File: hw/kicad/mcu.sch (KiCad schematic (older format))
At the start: 38 parts

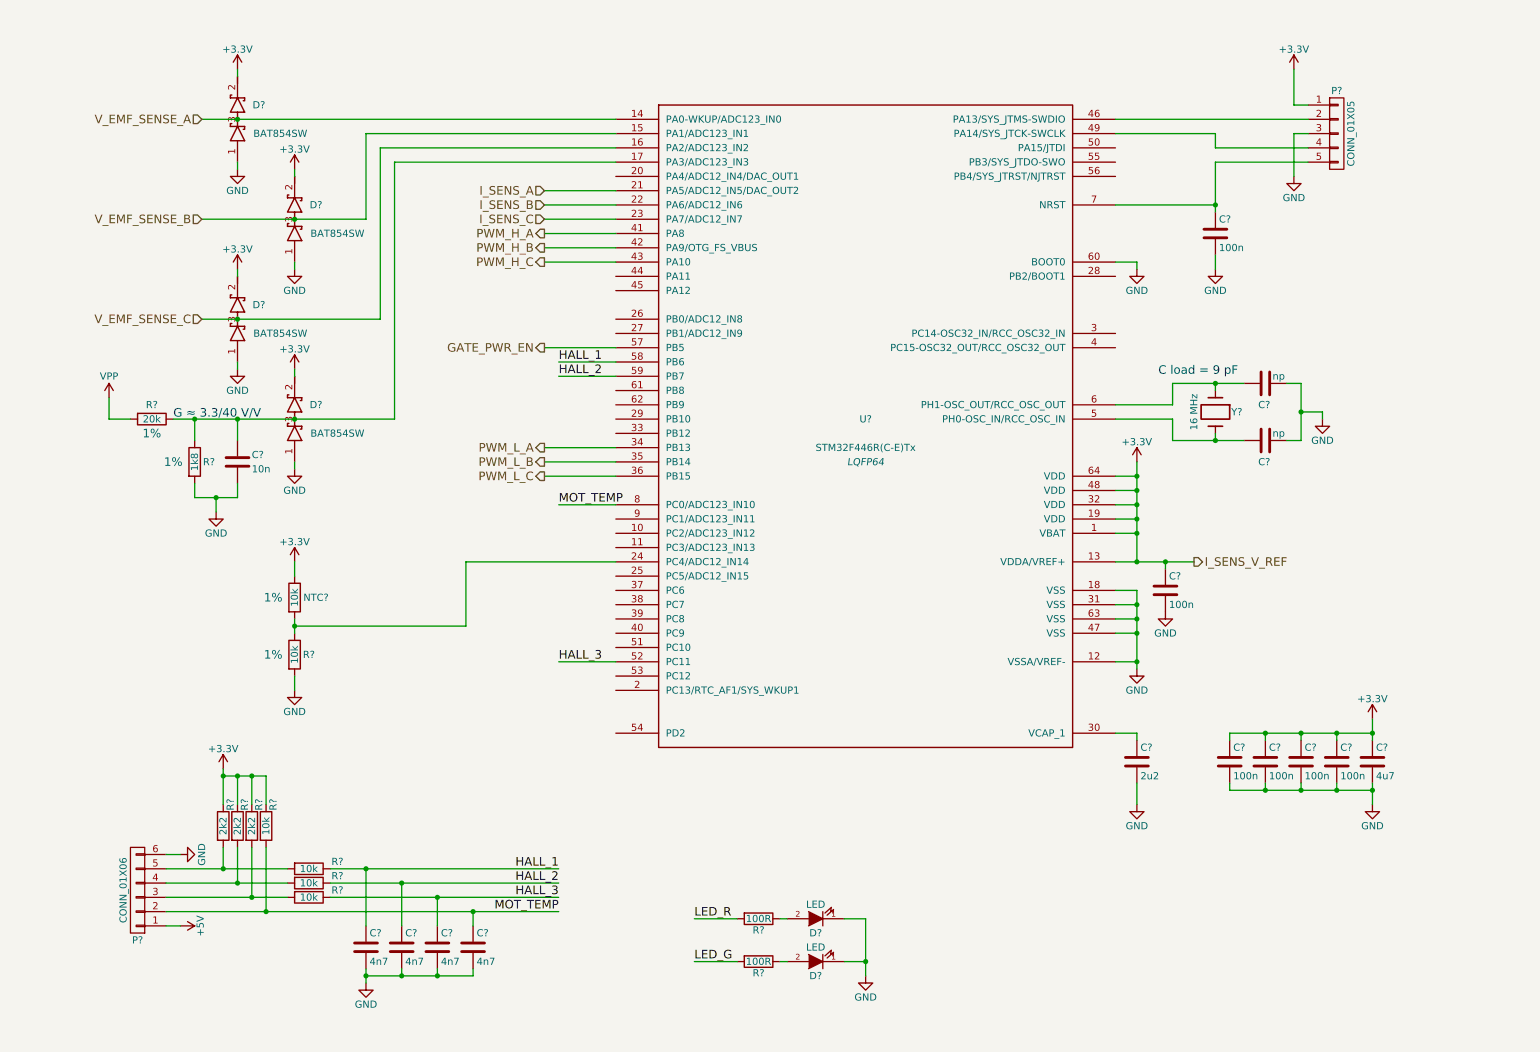
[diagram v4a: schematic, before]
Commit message: Connected and shuffled around mcu pins
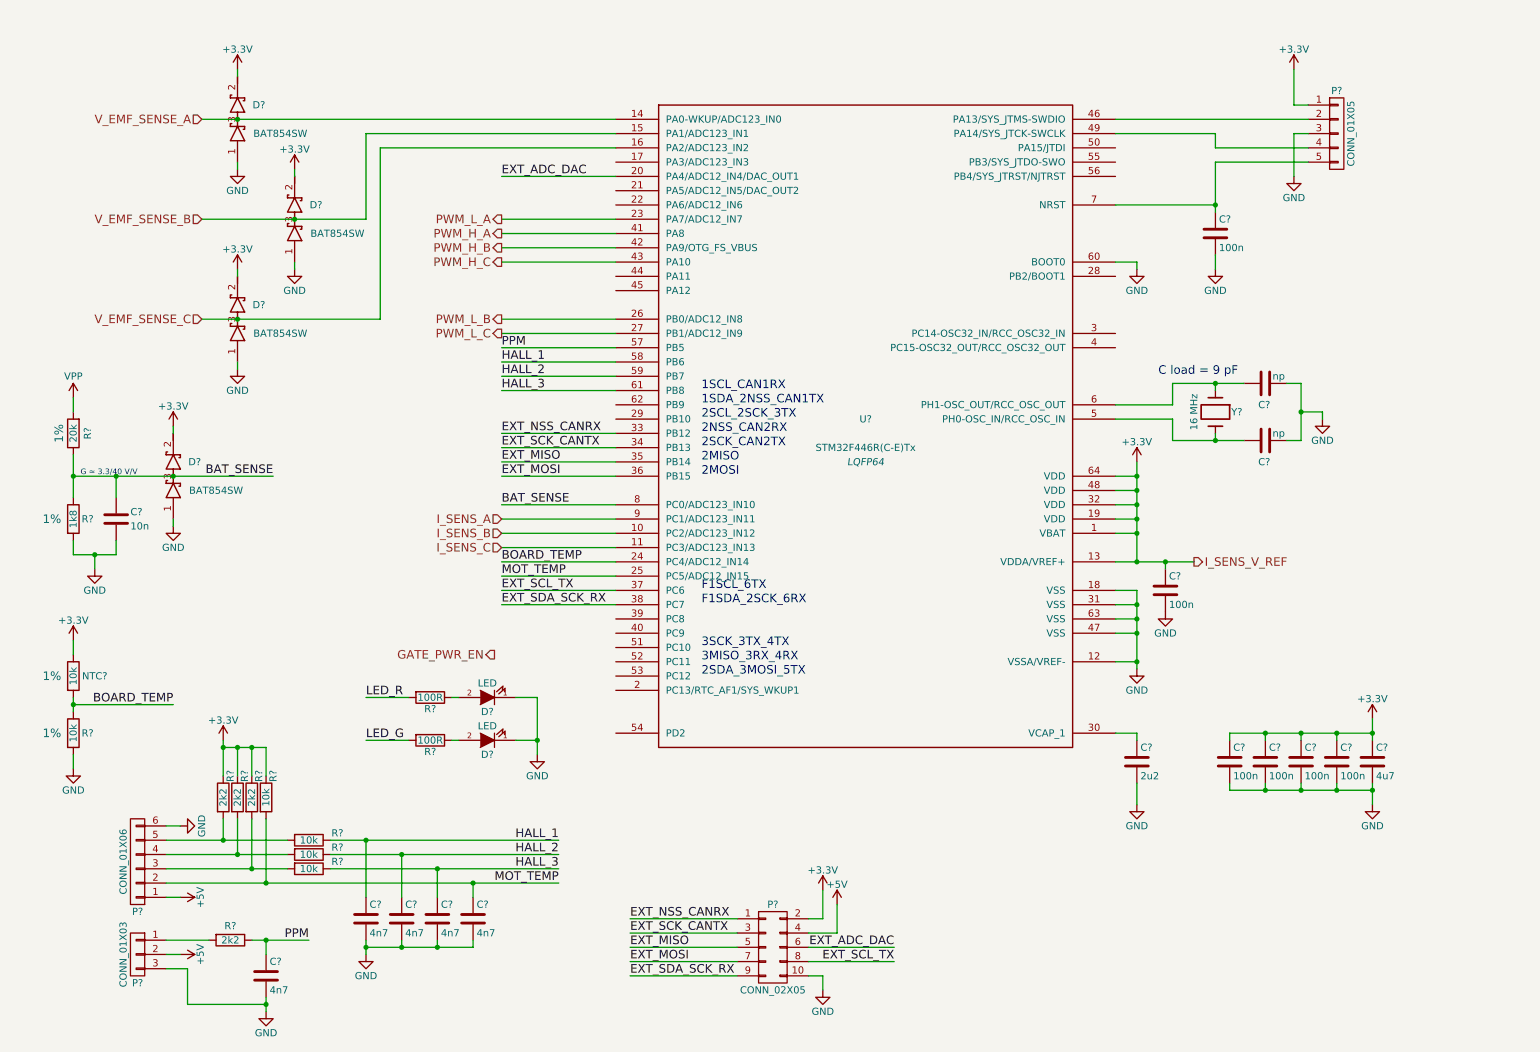
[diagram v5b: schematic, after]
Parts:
- added C?: 4n7, symbol C
- added P?: CONN_01X03, symbol CONN_01X03
- added P?: CONN_02X05, symbol CONN_02X05
- added R?: 2k2, symbol R
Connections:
- net +3V3: now also P?.2 (P2)
- net +5V: now also P?.2 (P2), P?.4 (P4)
- net GATE_PWR_EN: no longer U?.57 (PB5)
- net GND: now also C?.2, P?.10 (P10), P?.3 (P3)
- net HALL_3: now also U?.61 (PB8); no longer U?.52 (PC11)
- net I_SENS_A: now also U?.9 (PC1/ADC123_IN11); no longer U?.21 (PA5/ADC12_IN5/DAC_OUT2)
- net I_SENS_B: now also U?.10 (PC2/ADC123_IN12); no longer U?.22 (PA6/ADC12_IN6)
- net I_SENS_C: now also U?.11 (PC3/ADC123_IN13); no longer U?.23 (PA7/ADC12_IN7)
- net MOT_TEMP: now also U?.25 (PC5/ADC12_IN15); no longer U?.8 (PC0/ADC123_IN10)
- net PWM_L_A: now also U?.23 (PA7/ADC12_IN7); no longer U?.34 (PB13)
- net PWM_L_B: now also U?.26 (PB0/ADC12_IN8); no longer U?.35 (PB14)
- net PWM_L_C: now also U?.27 (PB1/ADC12_IN9); no longer U?.36 (PB15)
- net BAT_SENSE: now reaches C?.1, D?.3 (common), R?.1, R?.1
- net BAT_SENSE: now also U?.8 (PC0/ADC123_IN10); no longer U?.17 (PA3/ADC123_IN3)
- net EXT_ADC_DAC: now reaches U?.20 (PA4/ADC12_IN4/DAC_OUT1)
- net EXT_ADC_DAC: now also P?.6 (P6)
- net BOARD_TEMP: now reaches NTC?.2, R?.1, U?.24 (PC4/ADC12_IN14)
- net EXT_NSS_CANRX: now reaches U?.33 (PB12)
- net EXT_NSS_CANRX: now also P?.1 (P1)
- net EXT_SCL_TX: now reaches U?.37 (PC6)
- net EXT_SCL_TX: now also P?.8 (P8)
- net EXT_SDA_SCK_RX: now reaches U?.38 (PC7)
- net EXT_SDA_SCK_RX: now also P?.9 (P9)
- new net: P?.1 (P1), R?.2
- new net EXT_MISO: P?.5 (P5), U?.35 (PB14)
- new net EXT_MOSI: P?.7 (P7), U?.36 (PB15)
- new net EXT_SCK_CANTX: P?.3 (P3), U?.34 (PB13)
- new net PPM: C?.1, R?.1, U?.57 (PB5)
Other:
- note added: "1SCL_CAN1RX"
- note added: "1SDA_2NSS_CAN1TX"
- note added: "2MISO"
- note added: "2MOSI"
- note added: "2NSS_CAN2RX"
- note added: "2SCK_CAN2TX"
- note added: "2SCL_2SCK_3TX"
- note added: "2SDA_3MOSI_5TX"
- note added: "3MISO_3RX_4RX"
- note added: "3SCK_3TX_4TX"
- note added: "F1SCL_6TX"
- note added: "F1SDA_2SCK_6RX"
- moved on the sheet: C?, D?, NTC?, P?, R?

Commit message: Annotation
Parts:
- gave numbers to parts that had none: 42

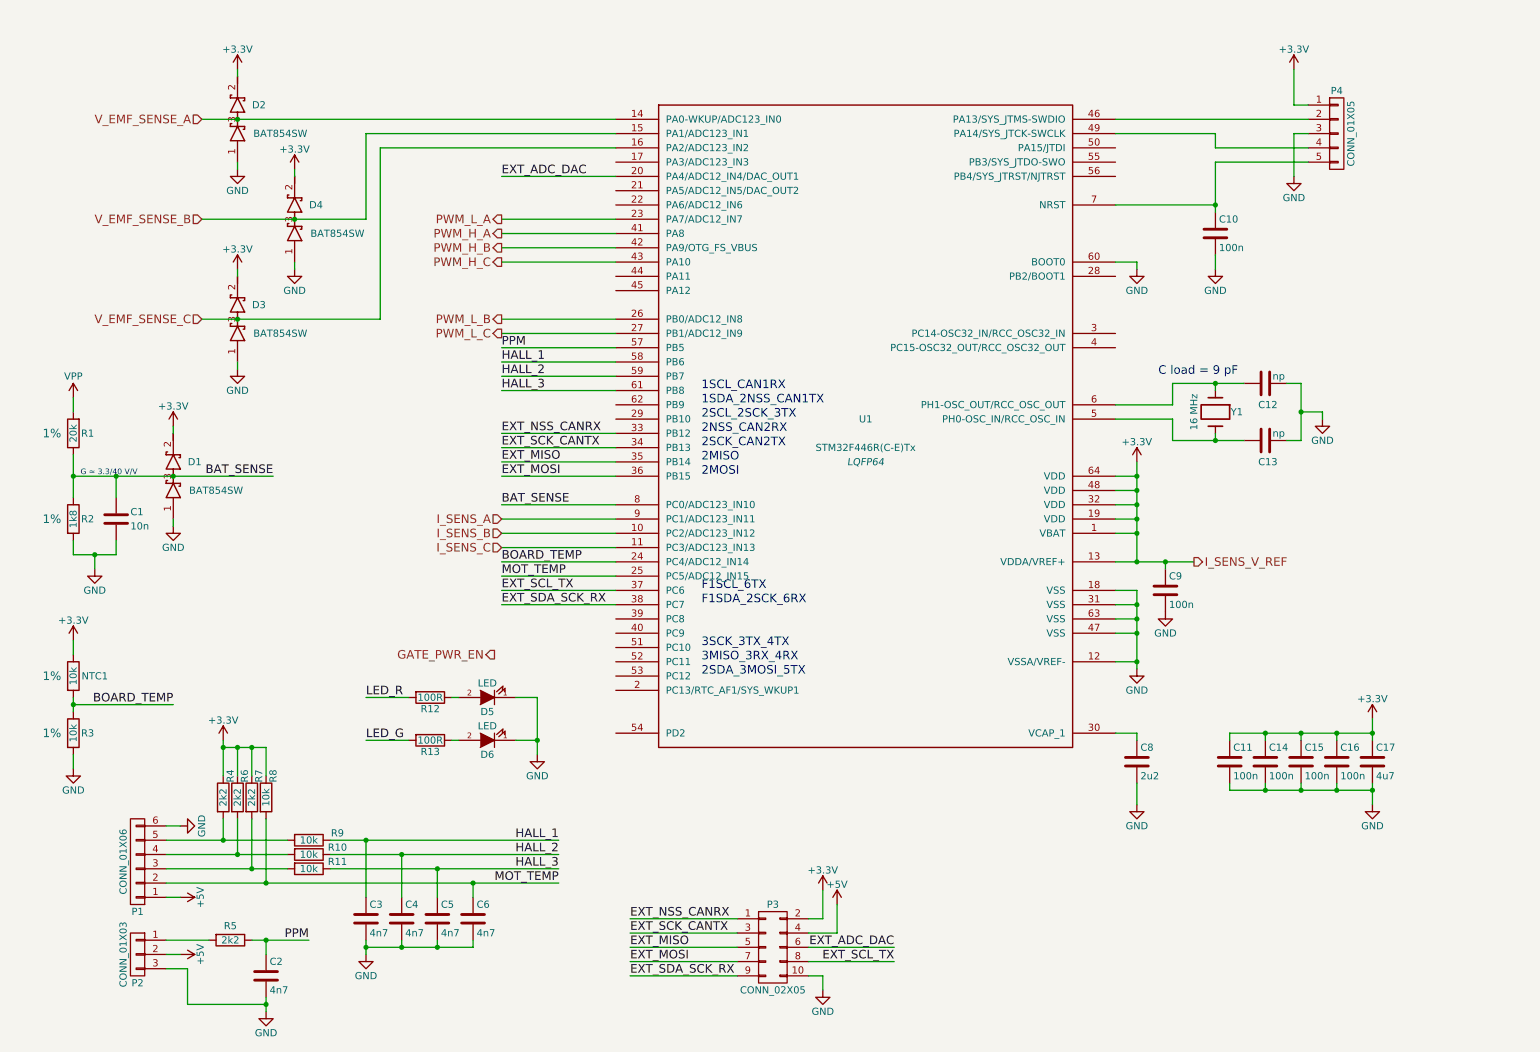
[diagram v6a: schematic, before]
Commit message: Map footprints to components and add BOM
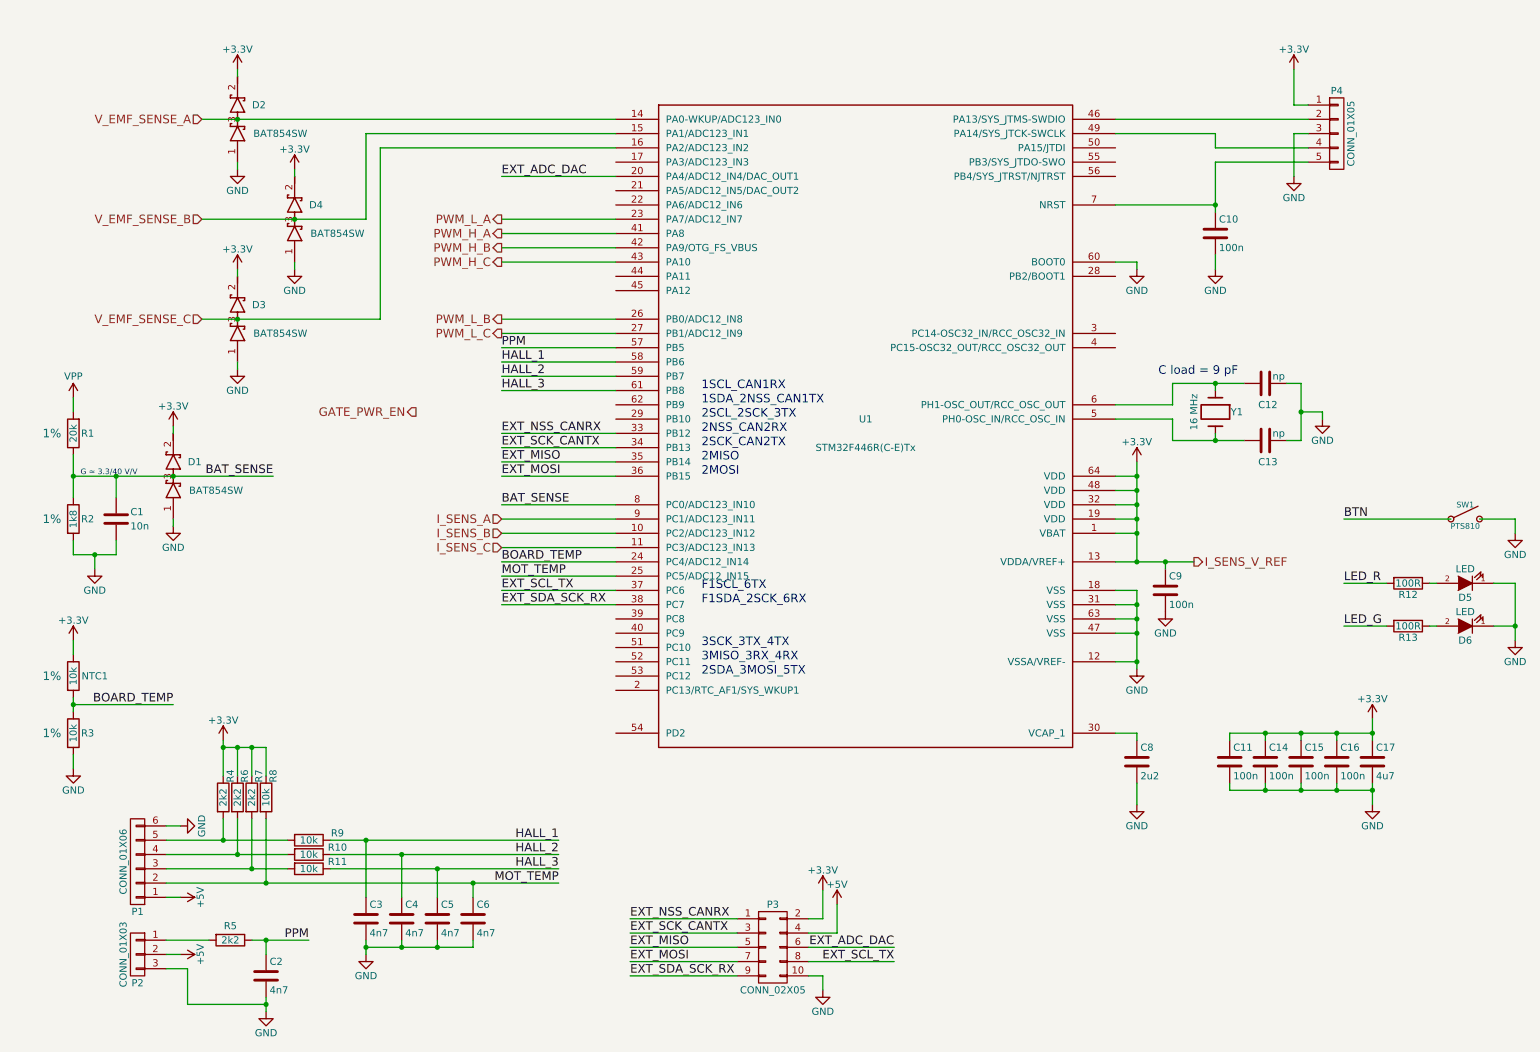
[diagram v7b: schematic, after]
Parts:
- added SW1: PTS810, electromechanical:PTS810, symbol PTS810
- C1, C10, C11, C12, C13, C14, C15, C16, C2, C3, C4, C5, C6, C8, C9: footprint (none) -> Capacitors_SMD:C_0402
- C17: footprint (none) -> Capacitors_SMD:C_0603
- D5, D6: footprint (none) -> LEDs:LED_0603
- P1: footprint (none) -> Pin_Headers:Pin_Header_Straight_1x06
- P2: footprint (none) -> Pin_Headers:Pin_Header_Straight_1x03
- P3: footprint (none) -> Pin_Headers:Pin_Header_Straight_2x05
- P4: footprint (none) -> Pin_Headers:Pin_Header_Straight_1x05
- R1, R10, R11, R12, R13, R2, R3, R4, R5, R6, R7, R8, R9: footprint (none) -> Resistors_SMD:R_0402
- U1: footprint LQFP64 -> Housings_QFP:LQFP-64_10x10mm_Pitch0.5mm
- Y1: footprint (none) -> Crystals:crystal_FA238-TSX3225
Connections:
- net GND: now also SW1.3, SW1.4
- new net BTN: SW1.1, SW1.2
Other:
- moved on the sheet: D5, D6, R12, R13
